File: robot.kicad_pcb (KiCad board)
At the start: 2 copper layers, 56.3 x 118.2 mm, 81 parts, among them J1 PCA9865 2, J10 Servo pwr, J11 Vin, J12 I2C, J13 VCC, J2 I2S, J3 Programming, J4 IMU, J5 Switches, J6 Expansion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

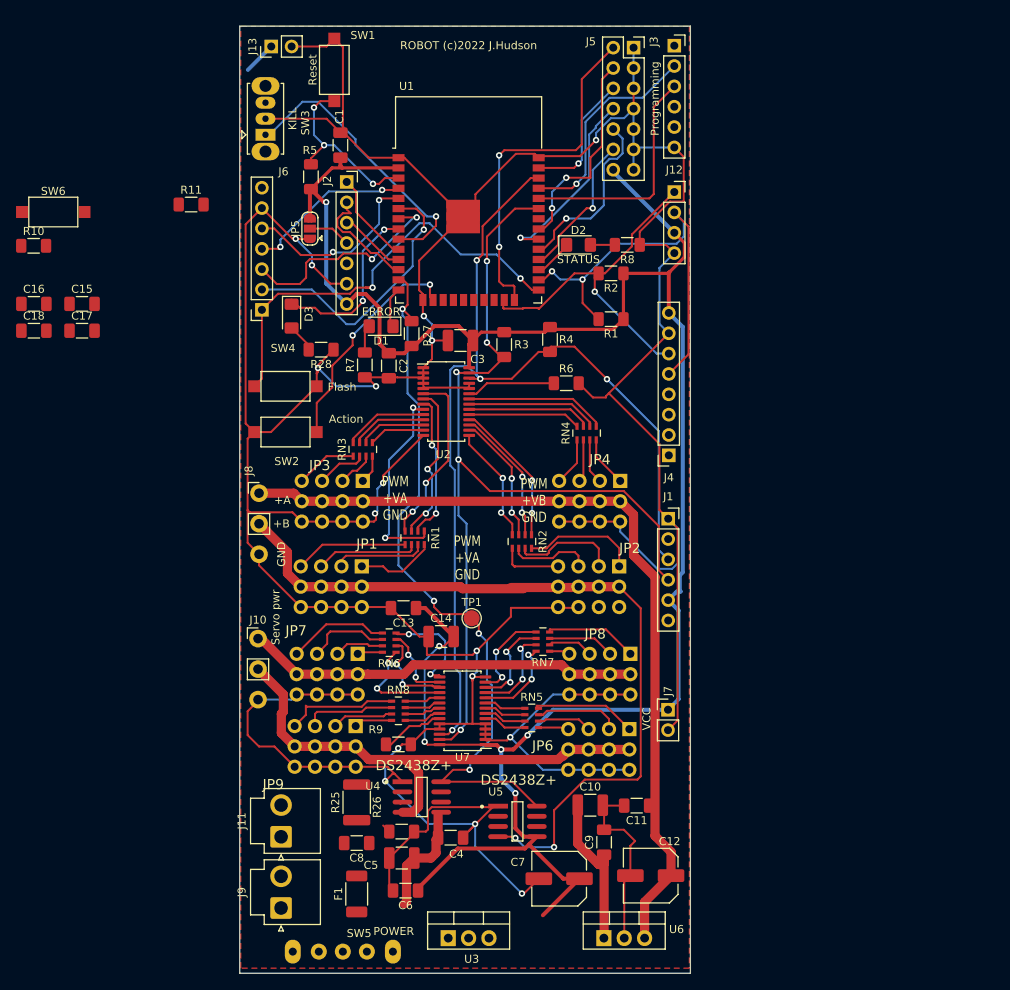
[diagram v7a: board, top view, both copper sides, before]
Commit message: Removed old ESP32, added ESP32 S3.
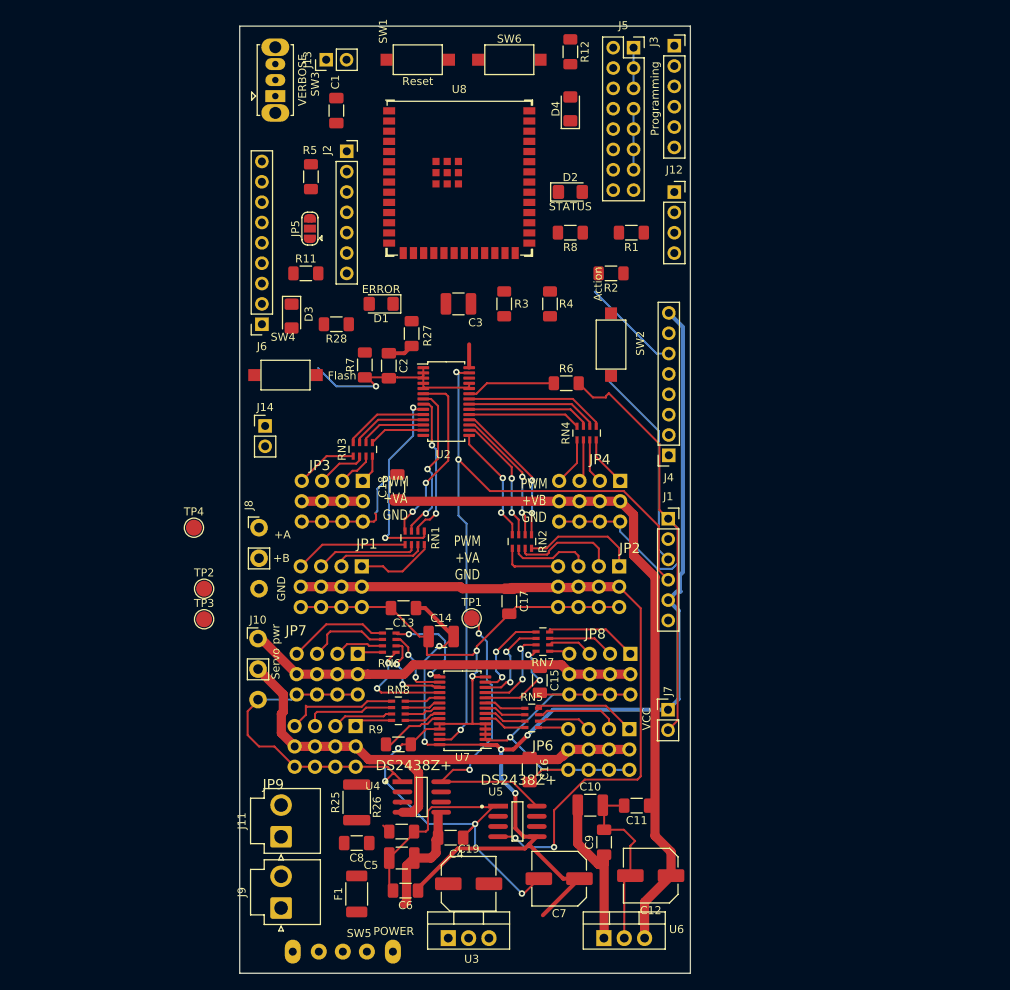
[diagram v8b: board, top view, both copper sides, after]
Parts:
- removed R10: 10K, Resistor_SMD:R_1206_3216Metric_Pad1.30x1.75mm_HandSolder
- removed U1: ESP32-WROOM-32D, RF_Module:ESP32-WROOM-32
- added C19: 470, Capacitor_SMD:C_Elec_6.3x7.7, F.Cu at (124.5, 199.4)
- added D4: BUSY, LED_SMD:LED_1206_3216Metric_Pad1.42x1.75mm_HandSolder, F.Cu at (137.2, 102.7)
- added J14: +5V, Connector_PinHeader_2.54mm:PinHeader_1x02_P2.54mm_Vertical, F.Cu at (99.1, 142.2)
- added R12: 470, Resistor_SMD:R_1206_3216Metric_Pad1.30x1.75mm_HandSolder, F.Cu at (137.2, 95.5)
- added TP2: +5V JOIN, TestPoint:TestPoint_Pad_D2.0mm, F.Cu at (91.4, 162.6)
- added TP3: +5V JOIN, TestPoint:TestPoint_Pad_D2.0mm, F.Cu at (91.4, 166.4)
- added TP4: +5V JOIN, TestPoint:TestPoint_Pad_D2.0mm, F.Cu at (90.2, 154.9)
- added U8: ESP32-S3-WROOM-1, PCM_Espressif:ESP32-S3-WROOM-1U, F.Cu at (123.3, 111.2)
- C12, C7: footprint Capacitor_SMD:C_Elec_6.3x5.8 -> Capacitor_SMD:C_Elec_6.3x5.4
- J5: footprint Connector_PinSocket_2.54mm:PinSocket_2x07_P2.54mm_Vertical -> Connector_PinSocket_2.54mm:PinSocket_2x08_P2.54mm_Vertical
- J6: footprint Connector_PinSocket_2.54mm:PinSocket_1x07_P2.54mm_Vertical -> Connector_PinSocket_2.54mm:PinSocket_1x09_P2.54mm_Vertical
- SW3: value KILL -> VERBOSE
- moved C16 84.9 mm to (132.1, 185.1), turned to -90 degrees
- moved C15 74.0 mm to (133.3, 174.0), turned to -90 degrees
- moved C17 63.1 mm to (129.5, 164.1), turned to -90 degrees
- moved SW6 60.0 mm to (129.5, 96.5)
- moved C18 49.4 mm to (115.6, 149.9), turned to 90 degrees
- moved SW2 42.1 mm to (142.2, 132.1), turned to -90 degrees
- moved R11 16.7 mm to (104.1, 123.2)
- moved R1 11.1 mm to (144.8, 118.1)
- moved SW1 10.5 mm to (118.1, 96.5), turned to 0 degrees
- moved R8 7.27 mm to (137.2, 118.1)
- moved J13 7.05 mm to (106.7, 96.5)
- moved D2 6.68 mm to (137.2, 113.0)
- moved R3 5.08 mm to (128.9, 127.0)
- moved SW3 4.98 mm to (100.3, 101.1)
- moved C3 4.58 mm to (123.2, 127.0)
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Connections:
- J5 pad 1: GND -> /SWITCH_7
- J5 pad 10: /SWITCH_1 -> /SWITCH_2
- J5 pad 12: /SWITCH_0 -> /SWITCH_1
- J5 pad 14: VCC -> /SWITCH_0
- J5 pad 2: /SWITCH_5 -> /SWITCH_6
- J5 pad 4: /SWITCH_4 -> /SWITCH_5
- J5 pad 6: /SWITCH_3 -> /SWITCH_4
- J5 pad 8: /SWITCH_2 -> /SWITCH_3
- J6 pad 2: IO_35 -> IO_11
- J6 pad 3: IO_36 -> IO_16
- J6 pad 4: IO_39 -> IO_40
- J6 pad 5: GND -> IO_42
- J6 pad 6: VCC -> IO_45
- J6 pad 7: (no net) -> IO_46
- SW6 pad 1: IO_34 -> IO_11
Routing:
- net GND: track 607.2 -> 376.5 mm, vias 16 -> 8
- net VCC: track 270.3 -> 158.3 mm, vias 6 -> 5
- net WIRE_1_SCL: track 127.9 -> 25.7 mm, vias 4 -> 0
- net IO_0: track 54.6 -> 0.00 mm, vias 2 -> 0
- net ONEWIRE_BUS: track 90.7 -> 38.5 mm, vias 4 -> 2
- net WIRE_0_SDA: track 51.8 -> 0.00 mm, vias 2 -> 0
- net /SWITCH_5: track 44.2 -> 0.00 mm, vias 2 -> 0
- net Net-(SW3-A): track 35.4 -> 0.00 mm, vias 1 -> 0
- net IO_34: track 34.0 -> 0.00 mm, vias 1 -> 0
- net WIRE_0_SCL: track 43.5 -> 12.4 mm, vias 1 -> 0
- net /ESP32_RX: track 29.1 -> 0.00 mm
- net WIRE_1_SDA: track 114.8 -> 85.9 mm, vias 5 -> 3
- net /SWITCH_ACTION: track 28.3 -> 0.00 mm, vias 2 -> 0
- net IO_35: track 27.3 -> 0.00 mm, vias 2 -> 0
- net /ESP32_TX: track 27.1 -> 0.00 mm, vias 1 -> 0
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- removed copper zone on F.Cu, net GND
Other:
- board text added: "ROBOT (c)2023 J.Hudson"
- board text removed: "ROBOT (c)2022 J.Hudson"
